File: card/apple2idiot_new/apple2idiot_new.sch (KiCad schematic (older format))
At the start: 9 parts, among them J1 AppleIIBus, J2 Conn_02x02_Odd_Even, J3 Conn_01x04, J4 Conn_02x02_Odd_Even, J5 Conn_02x02_Odd_Even, J6 Conn_02x07_Odd_Even, U1 IDT7132, U2 ESP32-DEVKITC-32D

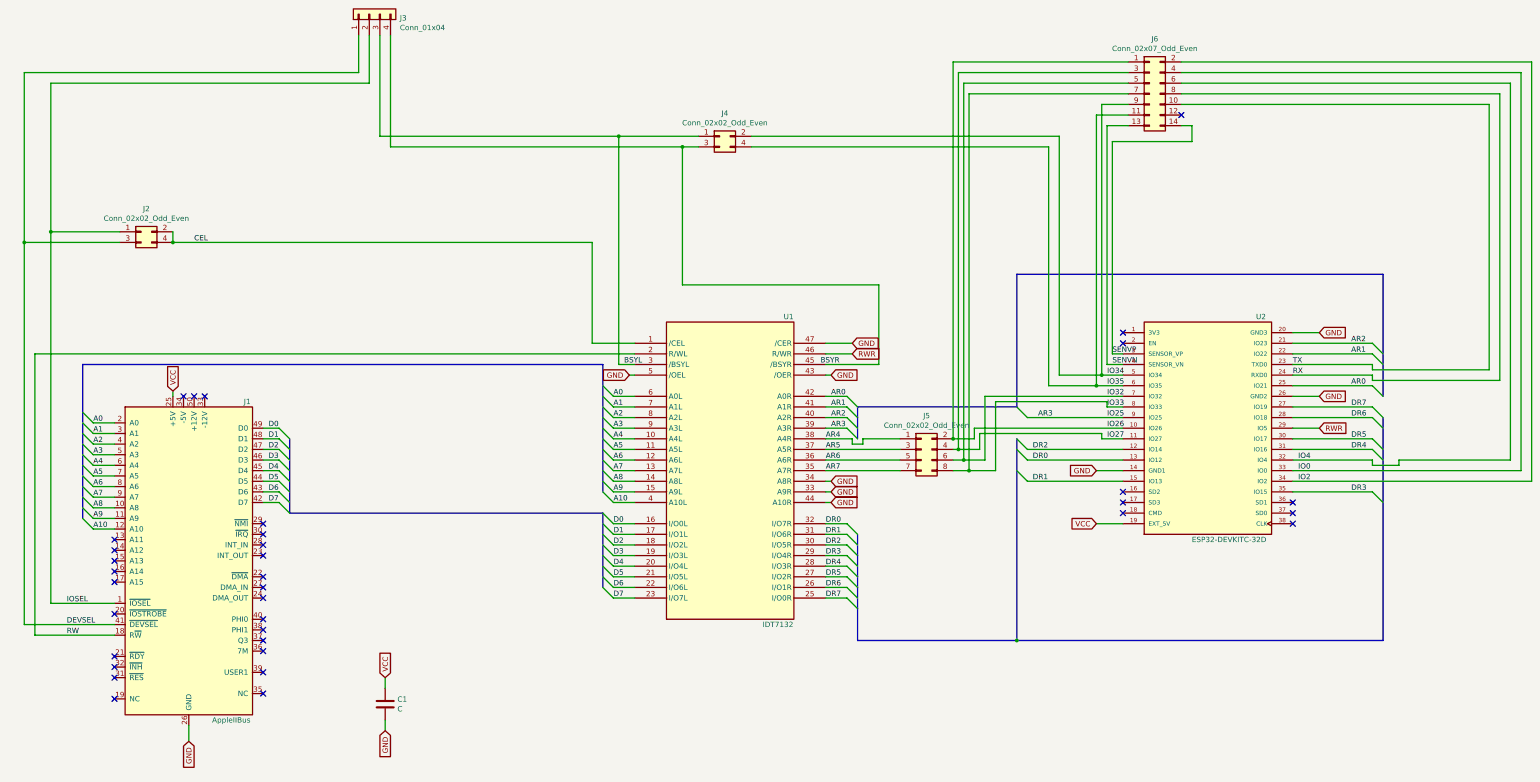
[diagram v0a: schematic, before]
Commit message: Card work: Diode, no more DEVSEL support, A8-10 grounded, and more
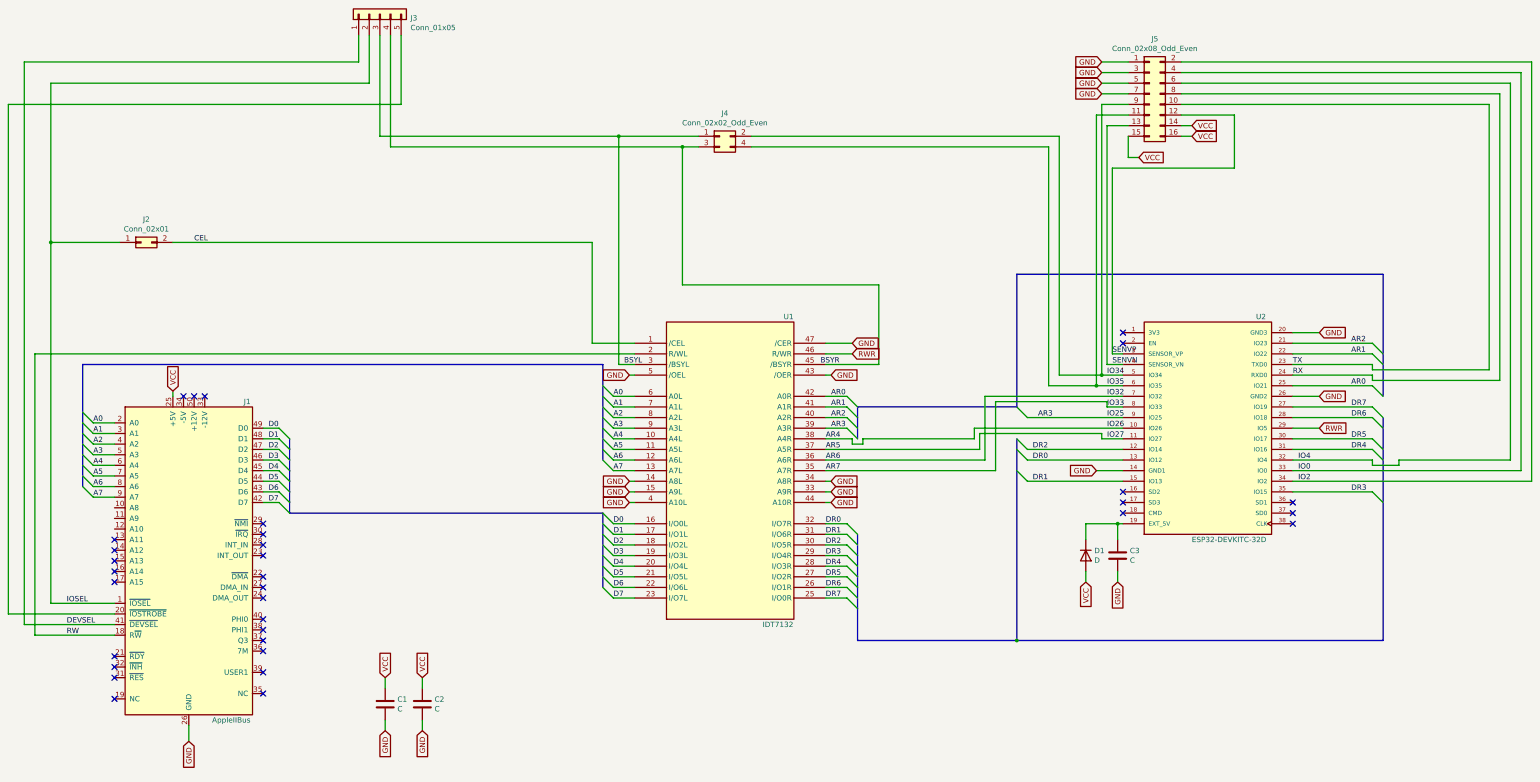
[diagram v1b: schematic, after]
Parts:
- removed J2: Conn_02x02_Odd_Even, Connector_PinHeader_2.54mm:PinHeader_2x02_P2.54mm_Vertical, symbol Connector_Generic:Conn_02x02_Odd_Even
- removed J3: Conn_01x04, Connector_PinSocket_2.54mm:PinSocket_1x04_P2.54mm_Vertical, symbol Connector_Generic:Conn_01x04
- removed J5: Conn_02x02_Odd_Even, Connector_PinHeader_2.54mm:PinHeader_2x04_P2.54mm_Vertical, symbol Connector_Generic:Conn_02x04_Odd_Even
- removed J6: Conn_02x07_Odd_Even, Connector_PinSocket_2.54mm:PinSocket_2x07_P2.54mm_Vertical, symbol Connector_Generic:Conn_02x07_Odd_Even
- added C2, C3: C, Capacitor_THT:C_Rect_L4.6mm_W2.0mm_P2.50mm_MKS02_FKP02, symbol Device:C
- added D1: D, Diode_THT:D_DO-41_SOD81_P10.16mm_Horizontal, symbol Device:D
- added J2: Conn_02x01, Connector_PinSocket_2.54mm:PinSocket_1x02_P2.54mm_Vertical, symbol Connector_Generic:Conn_02x01
- added J3: Conn_01x05, Connector_PinSocket_2.54mm:PinSocket_1x05_P2.54mm_Vertical, symbol Connector_Generic:Conn_01x05
- added J5: Conn_02x08_Odd_Even, Connector_PinSocket_2.54mm:PinSocket_2x08_P2.54mm_Vertical, symbol Connector_Generic:Conn_02x08_Odd_Even
- C1: footprint Capacitor_THT:C_Disc_D10.5mm_W5.0mm_P10.00mm -> Capacitor_THT:C_Rect_L4.6mm_W2.0mm_P2.50mm_MKS02_FKP02
- U2: footprint MODULE_ESP32-DEVKITC-32D -> ESPDEVKIT:MODULE_ESP32-DEVKITC-32D
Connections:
- net IO26 is gone; now on net AR4: U2.10 (IO26)
- net IO27 is gone; now on net AR5: U2.11 (IO27)
- net IO32 is gone; now on net AR6: U2.7 (IO32)
- net IO33 is gone; now on net AR7: U2.8 (IO33)
- net BSYL: now also J3.3 (Pin_3)
- net CEL: now also J2.2 (Pin_2)
- net DEVSEL: now also J3.1 (Pin_1)
- net GND: now also U1.14 (A8L), U1.15 (A9L), U1.4 (A10L), C2.2, C3.2, J5.1 (Pin_1), J5.3 (Pin_3), J5.5 (Pin_5), J5.7 (Pin_7)
- net IO0: now also J5.4 (Pin_4)
- net IO2: now also J5.2 (Pin_2)
- net IO34: now also J5.9 (Pin_9)
- net IO35: now also J5.11 (Pin_11)
- net IO4: now also J5.6 (Pin_6)
- net IOSEL: now also J2.1 (Pin_1), J3.2 (Pin_2)
- net RX: now also J5.8 (Pin_8)
- net SENVN: now also J5.13 (Pin_13)
- net SENVP: now also J5.12 (Pin_12)
- net TX: now also J5.10 (Pin_10)
- net VCC: now also C2.1, D1.2 (A), J5.14 (Pin_14), J5.15 (Pin_15), J5.16 (Pin_16); no longer U2.19 (EXT_5V)
- net at J1.20 (~IOSTROBE): now also J3.5 (Pin_5)
- net at J4.3 (Pin_3), U1.45 (/BSYR): now also J3.4 (Pin_4)
- net A10: no longer names the net of J1.12 (A10)
- net A10: no longer U1.4 (A10L)
- net A8: no longer names the net of J1.10 (A8)
- net A8: no longer U1.14 (A8L)
- net A9: no longer names the net of J1.11 (A9)
- net A9: no longer U1.15 (A9L)
- new net: C3.1, D1.1 (K), U2.19 (EXT_5V)
- no-connect marks 35 -> 33
